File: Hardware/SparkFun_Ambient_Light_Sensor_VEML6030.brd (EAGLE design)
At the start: 25.4 x 25.4 mm, 49 parts, among them U1 VEML6030

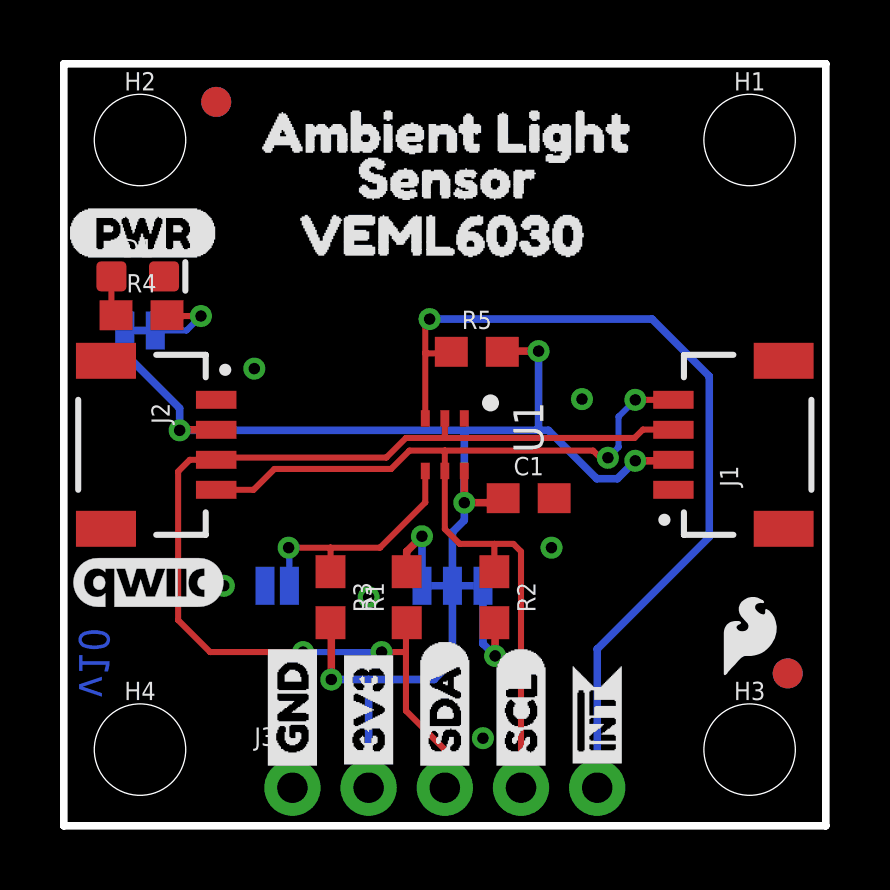
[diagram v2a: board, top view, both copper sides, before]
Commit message: Updates address silk for better clarificaiton, moves 3.3V trace to top near PTH for better ground pour
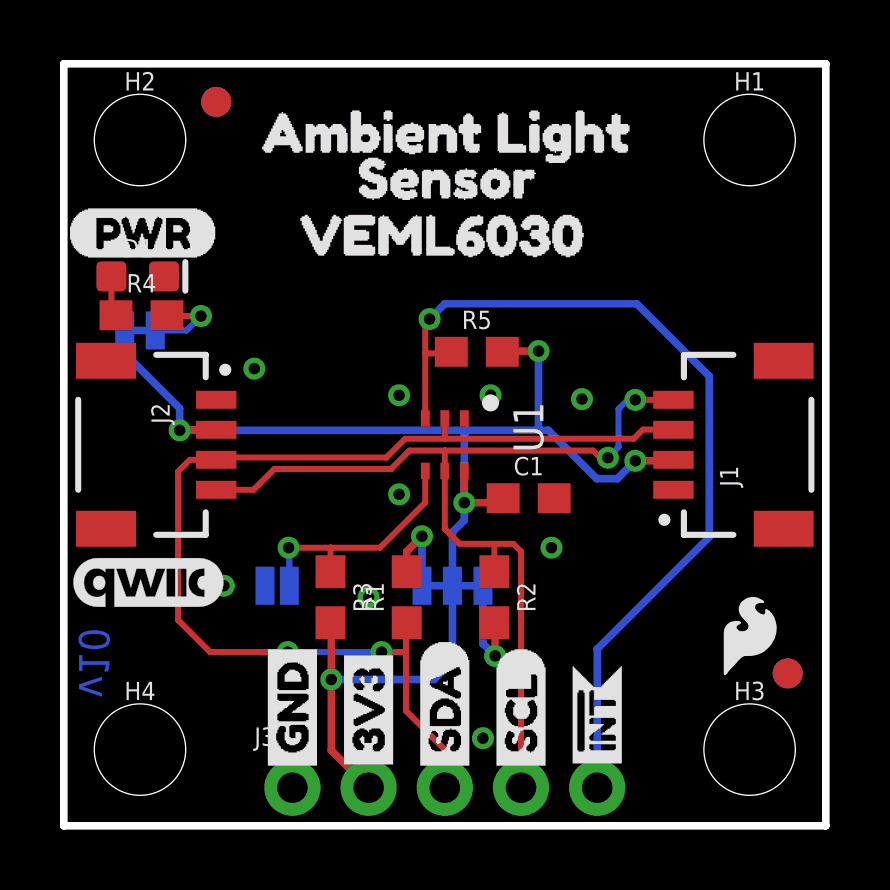
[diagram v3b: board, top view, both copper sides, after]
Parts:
- removed U$23: (no value), Address text:JUMPER#3
- added U$25: (no value), ADR:ADR0
- added U$26: (no value), ADR:JUMPER1
- U$20: device Address text:ADDRESSES4 -> ADR:CLOSED#2
- moved U$20 3.74 mm to (16.1, 12.8)
- moved U$24 0.60 mm to (9.60, 12.7)
- moved U$22 0.49 mm to (9.80, 14.3)
- moved U$21 0.37 mm to (16.1, 14.3)
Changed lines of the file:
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@@
 <layer number="115" name="ReferenceISLANDS" color="7" fill="1" visible="no" active="no"/>
 <layer number="116" name="Patch_BOT" color="9" fill="4" visible="no" active="no"/>
-<layer number="117" name="PM_Ref" color="26" fill="1" visible="no" active="yes"/>
+<layer number="117" name="PM_Ref" color="26" fill="1" visible="yes" active="yes"/>
 <layer number="118" name="Rect_Pads" color="7" fill="1" visible="no" active="no"/>
-<layer number="119" name="PF_Ref" color="31" fill="1" visible="no" active="yes"/>
-<layer number="120" name="WFL_Ref" color="25" fill="1" visible="no" active="yes"/>
+<layer number="119" name="PF_Ref" color="31" fill="1" visible="yes" active="yes"/>
+<layer number="120" name="WFL_Ref" color="25" fill="1" visible="yes" active="yes"/>
 <layer number="121" name="_tsilk" color="7" fill="1" visible="no" active="no"/>
 <layer number="122" name="_bsilk" color="7" fill="1" visible="no" active="no"/>
@@
 <dimension x1="0" y1="0" x2="0" y2="25.4" x3="-3.81" y3="12.7" textsize="1.778" textratio="7" layer="47" unit="inch" visible="yes"/>
 <dimension x1="2.54" y1="22.86" x2="2.54" y2="25.4" x3="-1.27" y3="24.13" textsize="1.778" textratio="7" layer="47" unit="inch" visible="yes"/>
-<wire x1="15.24" y1="17.018" x2="15.24" y2="11.684" width="0.2032" layer="22"/>
-<wire x1="15.24" y1="11.684" x2="4.826" y2="11.684" width="0.2032" layer="22"/>
+<wire x1="15.748" y1="17.018" x2="15.748" y2="11.684" width="0.2032" layer="22"/>
+<wire x1="15.748" y1="11.684" x2="4.826" y2="11.684" width="0.2032" layer="22"/>
 <wire x1="4.826" y1="11.684" x2="4.826" y2="17.018" width="0.2032" layer="22"/>
-<wire x1="4.826" y1="17.018" x2="15.24" y2="17.018" width="0.2032" layer="22"/>
+<wire x1="4.826" y1="17.018" x2="15.748" y2="17.018" width="0.2032" layer="22"/>
 </plain>
 <attributes>
@@
 <element name="U$18" library="SparkFun-Aesthetics" package="SFE_LOGO_FLAME_.1" value="" x="22.86" y="6.35" smashed="yes"/>
 <element name="U$19" library="Labels" package="PWR-()-04" value="" x="0.127" y="19.7612" smashed="yes"/>
-<element name="U$22" library="Address text" package="0X481" value="" x="9.3218" y="14.3764" smashed="yes" rot="MR0"/>
-<element name="U$24" library="Address text" package="0X103" value="" x="9.1186" y="13.081" smashed="yes" rot="MR0"/>
-<element name="U$20" library="Address text" package="ADDRESSES4" value="" x="14.5542" y="16.1798" smashed="yes" rot="MR0"/>
-<element name="U$21" library="Address text" package="DEFAULT#2" value="" x="15.748" y="14.478" smashed="yes" rot="MR0"/>
-<element name="U$23" library="Address text" package="JUMPER#3" value="" x="15.748" y="13.208" smashed="yes" rot="MR0"/>
+<element name="U$22" library="Address text" package="0X481" value="" x="9.8044" y="14.2748" smashed="yes" rot="MR0"/>
+<element name="U$24" library="Address text" package="0X103" value="" x="9.6012" y="12.7254" smashed="yes" rot="MR0"/>
+<element name="U$21" library="Address text" package="DEFAULT#2" value="" x="16.0528" y="14.2748" smashed="yes" rot="MR0"/>
+<element name="U$25" library="ADR" package="ADR0" value="" x="16.002" y="16.002" smashed="yes" rot="MR0"/>
+<element name="U$26" library="ADR" package="JUMPER1" value="" x="11.7856" y="16.002" smashed="yes" rot="MR0"/>
+<element name="U$20" library="ADR" package="CLOSED#2" value="" x="16.0528" y="12.7508" smashed="yes" rot="MR0"/>
 </elements>
 <signals>
@@
 <via x="13.97" y="2.921" extent="1-16" drill="0.381"/>
 <via x="17.272" y="14.224" extent="1-16" drill="0.381"/>
+<via x="11.176" y="11.049" extent="1-16" drill="0.381"/>
+<via x="11.176" y="14.351" extent="1-16" drill="0.381"/>
+<via x="14.224" y="14.351" extent="1-16" drill="0.381"/>
 </signal>
 <signal name="3.3V">
@@
 <contactref element="R3" pad="2"/>
 <contactref element="R5" pad="2"/>
-<wire x1="10.16" y1="1.27" x2="10.16" y2="2.032" width="0.254" layer="16"/>
 <via x="19.05" y="12.1666" extent="1-16" drill="0.381"/>
 <wire x1="20.32" y1="12.2" x2="20.2866" y2="12.1666" width="0.254" layer="1"/>
@@
 <wire x1="13.35" y1="13.0706" x2="13.462" y2="13.1826" width="0.254" layer="16"/>
 <wire x1="12.954" y1="5.4864" x2="12.954" y2="8.001" width="0.254" layer="16"/>
-<wire x1="8.9154" y1="4.8768" x2="10.16" y2="4.8768" width="0.254" layer="16"/>
-<wire x1="10.16" y1="4.8768" x2="10.16" y2="1.3208" width="0.254" layer="16"/>
 <wire x1="10.16" y1="1.3208" x2="10.1346" y2="1.2954" width="0.254" layer="16"/>
-<wire x1="10.16" y1="4.8768" x2="12.3444" y2="4.8768" width="0.254" layer="16"/>
+<wire x1="8.9154" y1="4.8768" x2="12.3444" y2="4.8768" width="0.254" layer="16"/>
 <wire x1="12.3444" y1="4.8768" x2="12.954" y2="5.4864" width="0.254" layer="16"/>
 <wire x1="19.05" y1="12.1666" x2="18.4531" y2="11.5697" width="0.254" layer="16"/>
@@
 <wire x1="15.8242" y1="15.8242" x2="15.8242" y2="13.2588" width="0.254" layer="16"/>
 <wire x1="15.8242" y1="13.2588" x2="15.748" y2="13.1826" width="0.254" layer="16"/>
+<wire x1="8.9154" y1="4.8768" x2="8.9154" y2="2.5146" width="0.254" layer="1"/>
+<wire x1="8.9154" y1="2.5146" x2="10.16" y2="1.27" width="0.254" layer="1"/>
 </signal>
 <signal name="SCL">
@@
 <wire x1="17.8816" y1="12.2682" x2="17.643009375" y2="12.506790625" width="0.2032" layer="1"/>
 <via x="18.1356" y="12.2682" extent="1-16" drill="0.381"/>
-<wire x1="18.4912" y1="13.6398" x2="18.4912" y2="12.6238" width="0.2032" layer="16"/>
+<wire x1="18.4912" y1="13.8938" x2="18.4912" y2="12.6238" width="0.2032" layer="16"/>
 <wire x1="18.1356" y1="12.2682" x2="18.4912" y2="12.6238" width="0.2032" layer="16"/>
-<wire x1="18.4912" y1="13.6398" x2="19.05" y2="14.1986" width="0.2032" layer="16"/>
+<wire x1="18.796" y1="14.1986" x2="18.4912" y2="13.8938" width="0.2032" layer="16"/>
+<wire x1="18.796" y1="14.1986" x2="19.05" y2="14.1986" width="0.2032" layer="16"/>
 <wire x1="12.7" y1="12.506790625" x2="17.643009375" y2="12.506790625" width="0.2032" layer="1"/>
 <wire x1="12.7" y1="9.8924" x2="12.7" y2="11.83" width="0.2032" layer="1"/>
@@
 <wire x1="4.199" y1="12.2" x2="3.81" y2="11.811" width="0.2032" layer="1"/>
 <wire x1="3.81" y1="11.811" x2="3.81" y2="6.858" width="0.2032" layer="1"/>
-<wire x1="4.8768" y1="5.7912" x2="7.9756" y2="5.7912" width="0.2032" layer="1"/>
+<wire x1="4.8768" y1="5.7912" x2="7.4676" y2="5.7912" width="0.2032" layer="1"/>
 <wire x1="3.81" y1="6.858" x2="4.8768" y2="5.7912" width="0.2032" layer="1"/>
-<via x="7.9756" y="5.7912" extent="1-16" drill="0.381"/>
+<via x="7.4676" y="5.7912" extent="1-16" drill="0.381"/>
 <wire x1="12.7" y1="2.54" x2="12.7" y2="1.27" width="0.2032" layer="1"/>
 <wire x1="12.7" y1="2.54" x2="11.4046" y2="3.8354" width="0.2032" layer="1"/>
-<wire x1="10.7522" y1="12.2762" x2="11.4046" y2="12.9286" width="0.2032" layer="1"/>
+<wire x1="10.7522" y1="12.2762" x2="11.3792" y2="12.9032" width="0.2032" layer="1"/>
 <wire x1="5.08" y1="12.2" x2="5.1562" y2="12.2762" width="0.2032" layer="1"/>
 <wire x1="10.7522" y1="12.2762" x2="5.1562" y2="12.2762" width="0.2032" layer="1"/>
-<wire x1="19.0246" y1="12.9286" x2="19.304" y2="13.208" width="0.2032" layer="1"/>
+<wire x1="18.9992" y1="12.9032" x2="19.304" y2="13.208" width="0.2032" layer="1"/>
 <wire x1="19.304" y1="13.208" x2="20.312" y2="13.208" width="0.2032" layer="1"/>
 <wire x1="20.312" y1="13.208" x2="20.32" y2="13.2" width="0.2032" layer="1"/>
-<wire x1="11.4046" y1="12.9286" x2="12.7" y2="12.9286" width="0.2032" layer="1"/>
-<wire x1="12.7" y1="12.9286" x2="19.0246" y2="12.9286" width="0.2032" layer="1"/>
-<wire x1="12.7" y1="13.58" x2="12.7" y2="12.9286" width="0.2032" layer="1"/>
-<wire x1="10.5918" y1="5.7912" x2="7.9756" y2="5.7912" width="0.2032" layer="16"/>
+<wire x1="11.3792" y1="12.9032" x2="12.7" y2="12.9032" width="0.2032" layer="1"/>
+<wire x1="12.7" y1="12.9032" x2="18.9992" y2="12.9032" width="0.2032" layer="1"/>
+<wire x1="12.7" y1="13.58" x2="12.7" y2="12.9032" width="0.2032" layer="1"/>
+<wire x1="10.5918" y1="5.7912" x2="7.4676" y2="5.7912" width="0.2032" layer="16"/>
 <via x="10.5918" y="5.7912" extent="1-16" drill="0.381"/>
 <wire x1="11.4046" y1="3.8354" x2="11.4046" y2="5.7912" width="0.2032" layer="1"/>
@@
 <wire x1="17.78" y1="5.8928" x2="21.5138" y2="9.6266" width="0.254" layer="16"/>
 <wire x1="21.5138" y1="9.6266" x2="21.5138" y2="14.986" width="0.254" layer="16"/>
-<wire x1="19.6088" y1="16.891" x2="12.192" y2="16.891" width="0.254" layer="16"/>
+<wire x1="19.1008" y1="17.399" x2="12.7" y2="17.399" width="0.254" layer="16"/>
+<wire x1="12.7" y1="17.399" x2="12.192" y2="16.891" width="0.254" layer="16"/>
 <via x="12.192" y="16.891" extent="1-16" drill="0.381"/>
-<wire x1="21.5138" y1="14.986" x2="19.6088" y2="16.891" width="0.254" layer="16"/>
+<wire x1="21.5138" y1="14.986" x2="19.1008" y2="17.399" width="0.254" layer="16"/>
 <wire x1="12.05" y1="16.749" x2="12.192" y2="16.891" width="0.2032" layer="1"/>
 <wire x1="12.05" y1="13.58" x2="12.05" y2="15.748" width="0.2032" layer="1"/>
